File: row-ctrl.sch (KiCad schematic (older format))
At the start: 17 parts, among them Q1 PMV50XP, Q2 PMV50XP, Q3 PMV50XP, Q4 PMV50XP, Q5 PMV50XP, Q6 PMV50XP, Q7 PMV50XP, Q8 PMV50XP, U5 74HC138

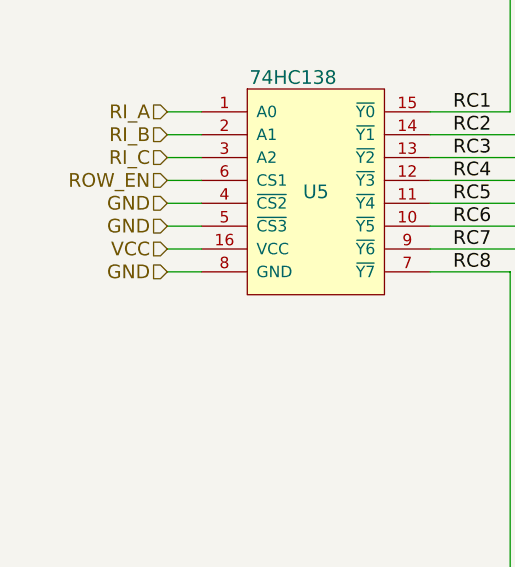
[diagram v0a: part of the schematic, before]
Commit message: add bypassing to schematic
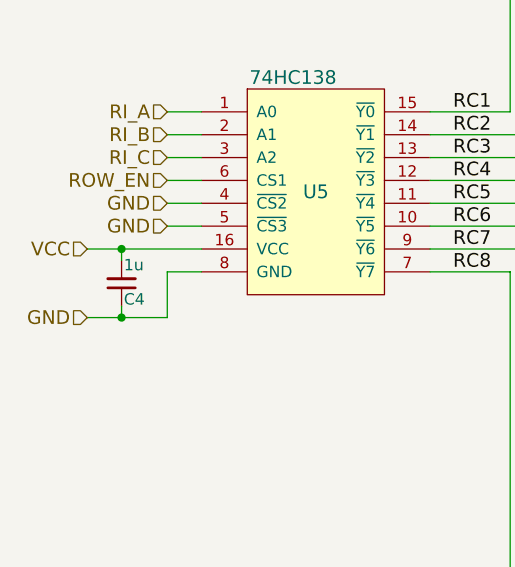
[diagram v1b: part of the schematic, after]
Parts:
- added C4: 1u, footprints:0603_HAND, symbol C_Small
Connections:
- net GND: now also C4.1
- net VCC: now also C4.2
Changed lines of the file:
@@
 Text HLabel 2900 4200 0    60   Input ~ 0
 GND
-Text HLabel 2900 4400 0    60   Input ~ 0
+Text HLabel 2550 4600 0    60   Input ~ 0
 GND
-Text HLabel 2900 4300 0    60   Input ~ 0
+Text HLabel 2550 4300 0    60   Input ~ 0
 VCC
 Wire Wire Line
@@
 	2900 4200 3050 4200
 Wire Wire Line
-	2900 4300 3050 4300
+	2550 4300 3050 4300
 Wire Wire Line
 	2900 4400 3050 4400
@@
 Wire Wire Line
 	4400 4400 4400 6650
+$Comp
+L C_Small C4
+U 1 1 59AC0042
+P 2700 4450
+F 0 "C4" H 2710 4520 50  0000 L CNN
+F 1 "1u" H 2710 4370 50  0000 L CNN
+F 2 "footprints:0603_HAND" H 2700 4450 50  0001 C CNN
+F 3 "" H 2700 4450 50  0001 C CNN
+	1    2700 4450
+	1    0    0    1
+$EndComp
+Wire Wire Line
+	2700 4350 2700 4300
+Connection ~ 2700 4300
+Wire Wire Line
+	2550 4600 2900 4600
+Wire Wire Line
+	2700 4600 2700 4550
+Wire Wire Line
+	2900 4600 2900 4400
+Connection ~ 2700 4600
 $EndSCHEMATC
